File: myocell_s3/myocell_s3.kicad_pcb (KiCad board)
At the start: 4 copper layers, 52 x 71 mm, 100 parts, among them J1 Conn_01x08, J2 IN3P, J3 IN3N, J4 IN4P, J5 Battery Connector JC2, J6 IN4N, J7 USB_C_Receptacle_USB2.0_16P, J8 RLD, Q3 DMG3404L, SW1 SW_Push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

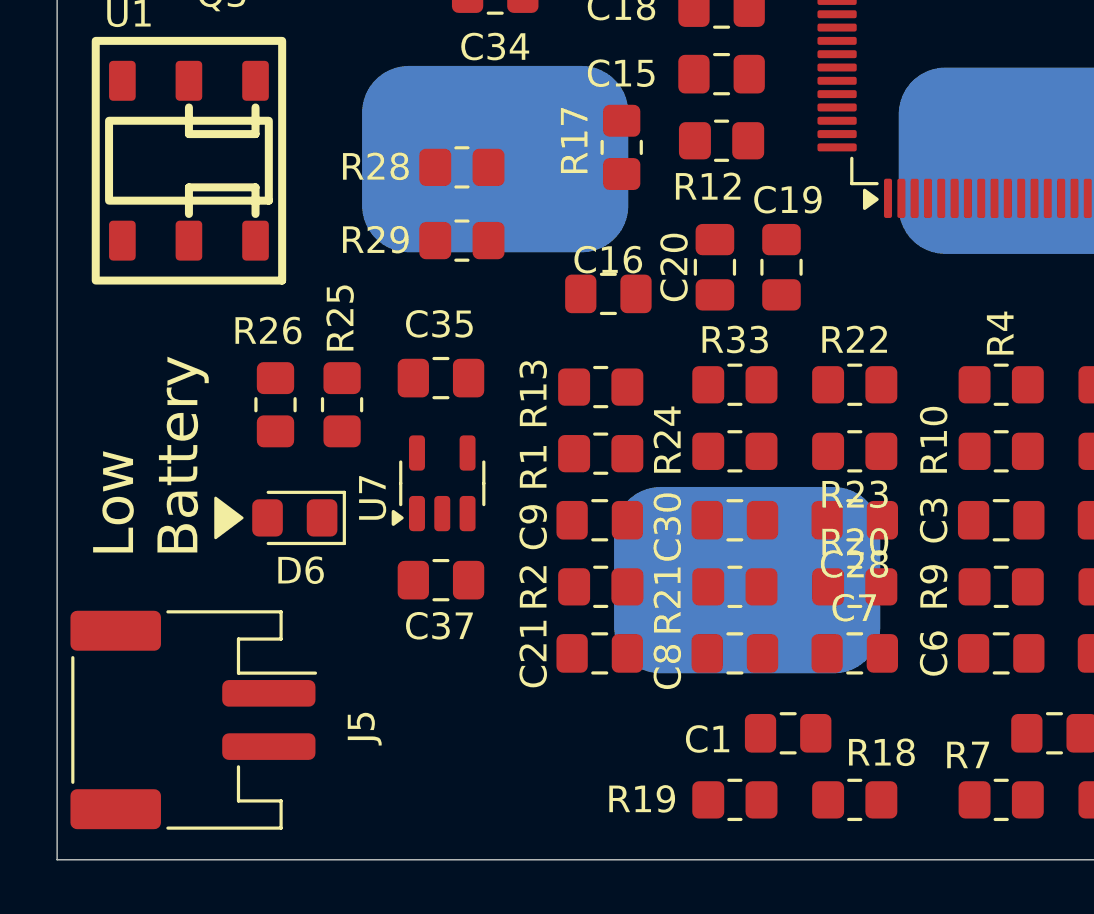
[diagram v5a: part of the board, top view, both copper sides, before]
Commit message: component placement
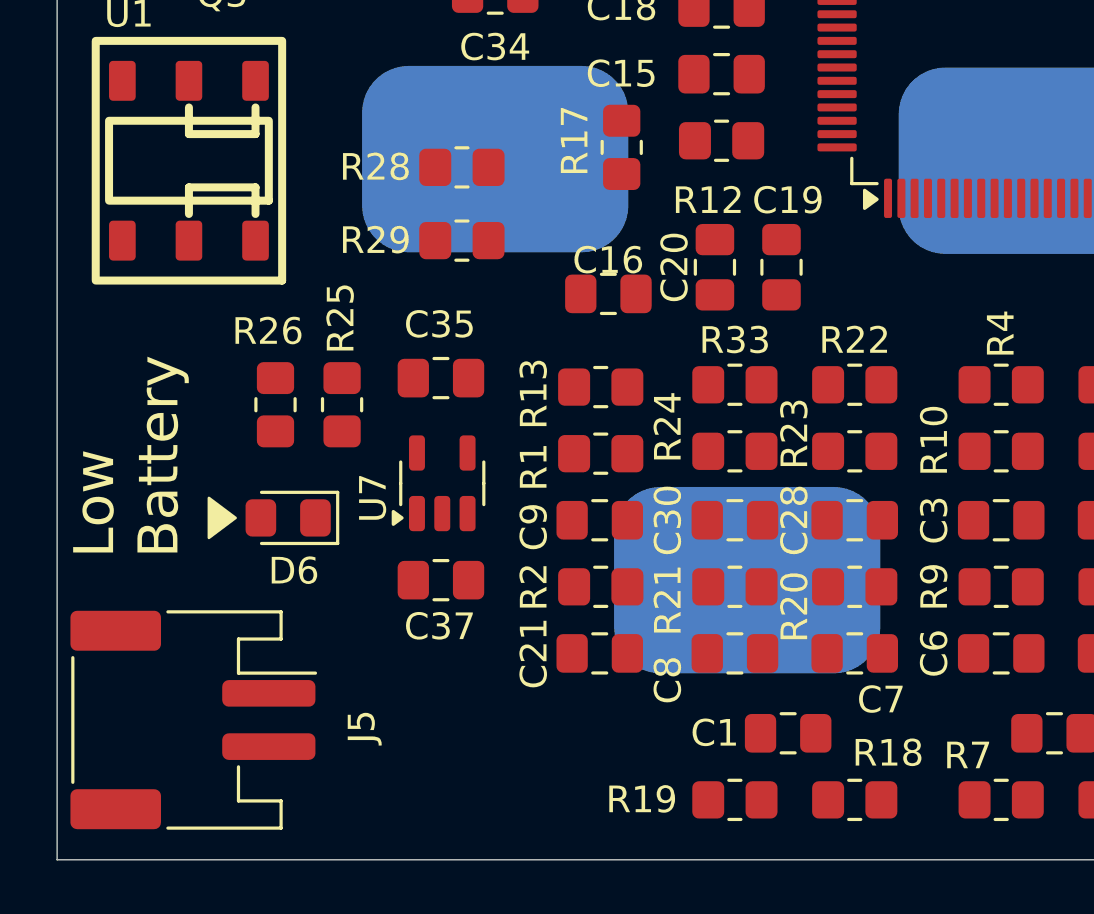
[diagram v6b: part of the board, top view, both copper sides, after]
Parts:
- moved D6 0.25 mm to (162.2, 108.2)
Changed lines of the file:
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@@
 		)
 		(property "Value" "1uF"
-			(at 7.2575 0.5 90)
+			(at -0.261252 -1.5 90)
 			(layer "F.Fab")
 			(effects
@@
 		(tags "resistor handsolder")
 		(property "Reference" "R18"
-			(at -1 1.75 0)
+			(at -1.25 1.75 0)
 			(layer "F.SilkS")
 			(effects
@@
 		(tags "capacitor handsolder")
 		(property "Reference" "C30"
-			(at -2.5 0.25 90)
+			(at -2.5 0 90)
 			(layer "F.SilkS")
 			(effects
@@
 		)
 		(property "Value" "0.1uF"
-			(at 0 1.68 0)
+			(at 2.5 0.25 90)
 			(layer "F.Fab")
 			(effects
@@
 		)
 		(property "Value" "0.01uF"
-			(at -4.25 -2.04 0)
+			(at -5.727064 -1.265 90)
 			(layer "F.Fab")
 			(effects
@@
 		)
 		(property "Value" "4.7uF"
-			(at 0 -5.72 0)
+			(at 0.0375 0.0875 90)
 			(layer "F.Fab")
 			(effects
@@
 		)
 		(fp_text user "${REFERENCE}"
-			(at 0 -3.72 0)
+			(at 0 0.0875 90)
 			(layer "F.Fab")
 			(effects
@@
 		)
 		(property "Value" "0.1uF"
-			(at 2.75 0 90)
+			(at 2.75 0.735 90)
 			(layer "F.Fab")
 			(effects
@@
 		)
 		(fp_text user "${REFERENCE}"
-			(at 0 3.72 0)
+			(at -0.0375 0 90)
 			(layer "F.Fab")
 			(effects
@@
 		)
 		(property "Value" "22k"
-			(at 0 1.65 0)
+			(at -0.227064 0 90)
 			(layer "F.Fab")
 			(effects
@@
 		(tags "resistor handsolder")
 		(property "Reference" "R12"
-			(at -0.5 1.75 0)
+			(at -0.5 2.25 0)
 			(layer "F.SilkS")
 			(effects
@@
 		)
 		(property "Value" "0"
-			(at 0 -2.07 0)
+			(at 0 0 0)
 			(layer "F.Fab")
 			(effects
@@
 		(tags "capacitor handsolder")
 		(property "Reference" "C8"
-			(at -2.5 0.5 90)
+			(at -2.5 1 90)
 			(layer "F.SilkS")
 			(effects
@@
 		)
 		(fp_text user "${REFERENCE}"
-			(at 3.72 0 90)
+			(at 0 0 180)
 			(layer "F.Fab")
 			(effects
@@
 		)
 		(property "Value" "390k"
-			(at 0 5.37 0)
+			(at -0.0375 0 90)
 			(layer "F.Fab")
 			(effects
@@
 		)
 		(property "Value" "1uF"
-			(at 0 5.4 0)
+			(at 0 0 0)
 			(layer "F.Fab")
 			(effects
@@
 		)
 		(fp_text user "${REFERENCE}"
-			(at 0 3.72 0)
+			(at 0 0 90)
 			(layer "F.Fab")
 			(effects
@@
 		)
 		(property "Value" "10k"
-			(at 0 5.37 0)
+			(at 0.227064 0 90)
 			(layer "F.Fab")
 			(effects
@@
 		)
 		(fp_text user "${REFERENCE}"
-			(at 0 3.72 0)
+			(at 0 0 90)
 			(layer "F.Fab")
 			(effects
@@
 		)
 		(property "Value" "2.2uF"
-			(at 3.9625 -0.5 90)
+			(at 2.4625 0.25 180)
 			(layer "F.Fab")
 			(effects
@@
 		)
 		(fp_text user "${REFERENCE}"
-			(at 3.72 0 90)
+			(at -0.0375 0 180)
 			(layer "F.Fab")
 			(effects
@@
 	(footprint "LED_SMD:LED_0805_2012Metric_Pad1.15x1.40mm_HandSolder"
 		(layer "F.Cu")
-		(at 162.475 108.1625 180)
+		(at 162.225 108.1625 180)
 		(descr "LED SMD 0805 (2012 Metric), square (rectangular) end terminal, IPC-7351 nominal, (Body size source: https://docs.google.com/spreadsheets/d/1BsfQQcO9C6DZCsRaXUlFlo91Tg2WpOkGARC1WS5S8t0/edit?usp=sharing), generated with kicad-footprint-generator")
 		(tags "LED handsolder")
@@
 		(tags "resistor handsolder")
 		(property "Reference" "R20"
-			(at 0 -1.65 0)
+			(at -2.25 0.75 90)
 			(layer "F.SilkS")
 			(effects
@@
 		)
 		(property "Value" "0.1uF"
-			(at 6.1825 0 0)
+			(at 0 0.25 0)
 			(layer "F.Fab")
 			(effects
@@
 		)
 		(fp_text user "${REFERENCE}"
-			(at 3.72 0 90)
+			(at 0 0 180)
 			(layer "F.Fab")
 			(effects
@@
 		(tags "resistor handsolder")
 		(property "Reference" "R24"
-			(at 2.5 0.4125 90)
+			(at 2.5 0.9125 90)
 			(layer "F.SilkS")
 			(effects
@@
 		)
 		(fp_text user "${REFERENCE}"
-			(at 3.72 0 90)
+			(at 0 0 180)
 			(layer "F.Fab")
 			(effects
@@
 		(tags "capacitor handsolder")
 		(property "Reference" "C7"
-			(at 0 -1.68 0)
+			(at 1 1.75 180)
 			(layer "F.SilkS")
 			(effects
@@
 		)
 		(property "Value" "4.7uF"
-			(at 0 1.68 0)
+			(at -0.2875 0 90)
 			(layer "F.Fab")
 			(effects
@@
 		(tags "capacitor handsolder")
 		(property "Reference" "C28"
-			(at 0 -1.68 0)
+			(at 2.25 0 90)
 			(layer "F.SilkS")
 			(effects
@@
 		)
 		(fp_text user "${REFERENCE}"
-			(at 3.72 0 90)
+			(at 0 0 180)
 			(layer "F.Fab")
 			(effects
@@
 		(tags "capacitor handsolder")
 		(property "Reference" "C1"
-			(at 3 -0.25 0)
+			(at 2.75 0 0)
 			(layer "F.SilkS")
 			(effects
@@
 		)
 		(property "Value" "20"
-			(at 0 1.65 0)
+			(at 0 -0.735 0)
 			(layer "F.Fab")
 			(effects
@@
 		(tags "resistor handsolder")
 		(property "Reference" "R23"
-			(at 0 -1.65 0)
+			(at 2.25 0.6625 90)
 			(layer "F.SilkS")
 			(effects
@@
 		(at 170 94.69 180)
 		(property "Reference" "J3"
-			(at -7.62 0 0)
+			(at -6.25 0 0)
 			(unlocked yes)
 			(layer "B.SilkS")
@@
 	(gr_poly
 		(pts
-			(xy 159.5 108.9125) (xy 159.5 107.4125) (xy 160.5 108.1625)
+			(xy 159.25 108.9125) (xy 159.25 107.4125) (xy 160.25 108.1625)
 		)
 		(stroke
@@
 	)
 	(gr_text "Low\nBattery"
-		(at 159 109.6625 90)
+		(at 158.25 109.6625 90)
 		(layer "F.SilkS")
 		(effects

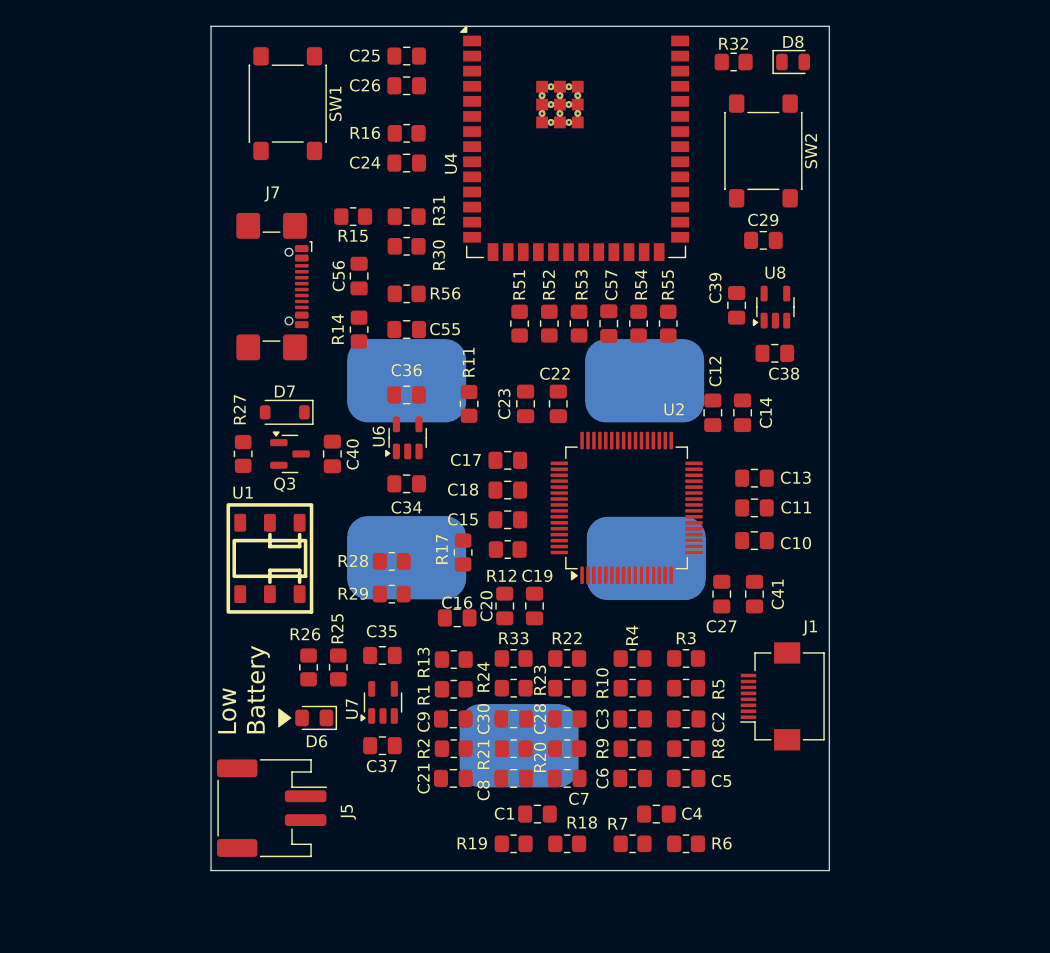
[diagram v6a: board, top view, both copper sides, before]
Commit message: drdy fixed
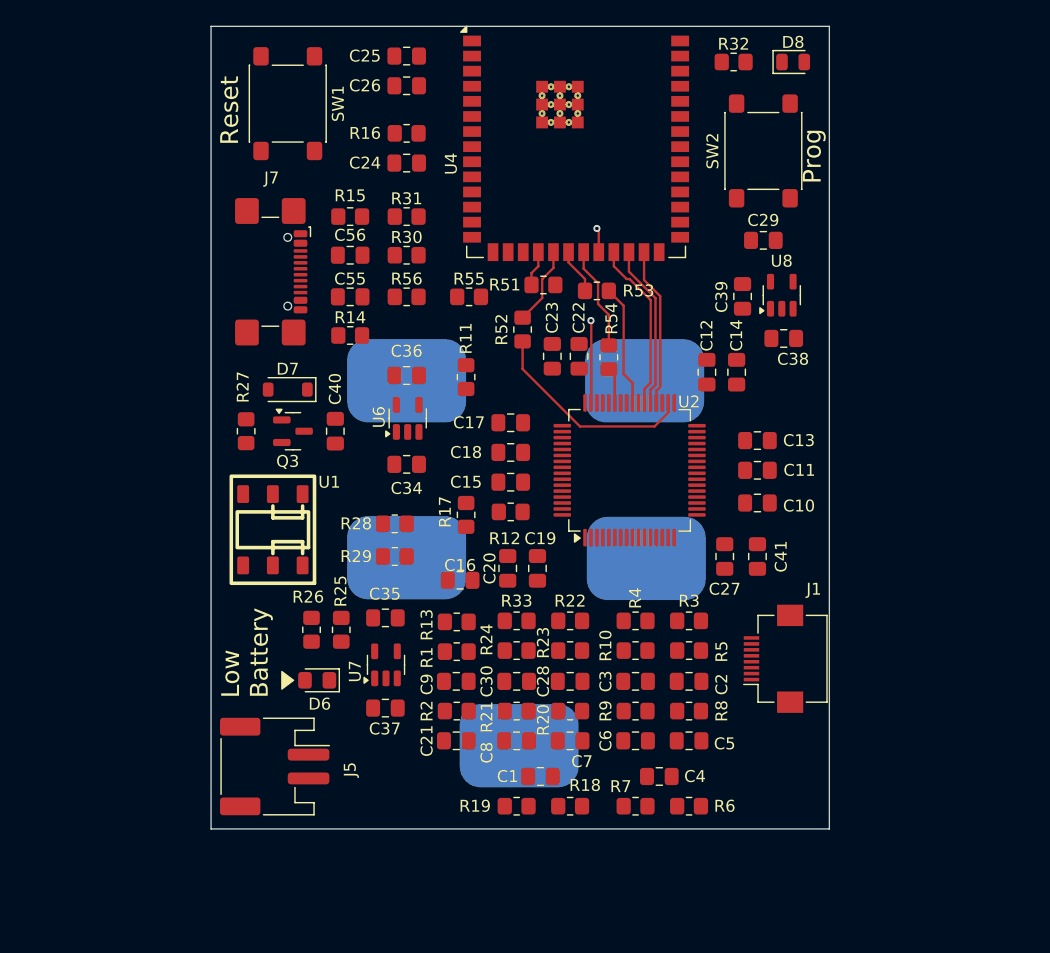
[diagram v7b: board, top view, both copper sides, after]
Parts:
- removed C57: 10pF, Capacitor_SMD:C_0805_2012Metric_Pad1.18x1.45mm_HandSolder
- moved R55 16.9 mm to (175.2, 72.8), turned to 0 degrees
- moved C55 5.49 mm to (165.2, 72.8)
- moved C23 4.59 mm to (182.2, 77.8)
- moved C22 4.37 mm to (184.5, 77.8)
- moved R51 3.82 mm to (181.5, 71.8), turned to 180 degrees
- moved R54 3.78 mm to (187.0, 77.8)
- moved J5 3.51 mm to (158.9, 112.2)
- moved C12 3.45 mm to (195.2, 79.1)
- moved C14 3.45 mm to (197.8, 79.1)
- moved C1 3.17 mm to (181.2, 113.1)
- moved C10 3.17 mm to (199.5, 90.1)
- moved C11 3.17 mm to (199.5, 87.3)
- moved C13 3.17 mm to (199.5, 84.8)
- moved C15 3.17 mm to (178.8, 88.3)
- moved C16 3.17 mm to (174.5, 96.6)
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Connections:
- U4 pad 22: unconnected-(U4-IO14-Pad22) -> /adc_8/drdy
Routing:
- net /adc_8/din: track 0.00 -> 17.9 mm
- net /adc_8/drdy: track 0.00 -> 17.0 mm, vias 0 -> 2
- net /adc_8/start: track 0.00 -> 14.3 mm
- net /adc_8/clk: track 0.00 -> 13.8 mm
- net /adc_8/reset: track 0.00 -> 13.4 mm
- net /adc_8/sclk: track 0.00 -> 10.3 mm
- net Net-(U4-IO13): track 0.00 -> 9.43 mm
- net Net-(U4-IO11): track 0.00 -> 6.93 mm
- net Net-(U4-IO12): track 0.00 -> 3.83 mm
- net /adc_8/dout: track 0.00 -> 3.04 mm
- net Net-(U4-IO10): track 0.00 -> 3.00 mm
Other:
- board size 52 x 71 mm -> 52 x 67.5 mm
- board text added: "Prog"
- board text added: "Reset"

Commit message: spi routed length aligned to 20mm/pm0.5mm
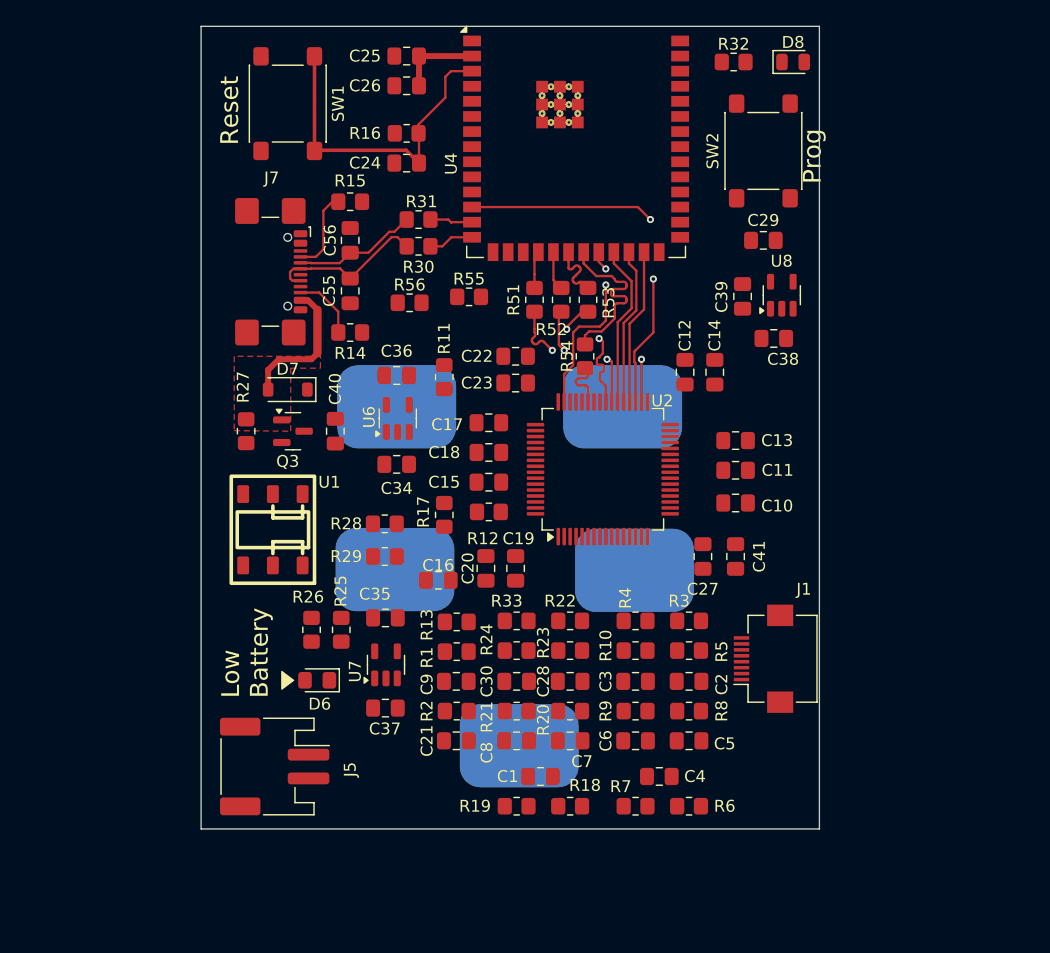
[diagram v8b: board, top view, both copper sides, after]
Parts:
- moved C22 5.34 mm to (179.2, 77.8), turned to 0 degrees
- moved R52 4.10 mm to (183.0, 73.0)
- moved C23 3.82 mm to (179.2, 80.0), turned to 0 degrees
- moved J4 2.87 mm to (188.2, 82.0)
- moved J2 2.34 mm to (169.2, 82.0)
- moved U2 2.25 mm to (186.5, 87.2)
- moved R54 2.00 mm to (185.0, 77.8)
- moved C10 1.84 mm to (197.7, 90.1)
- moved C11 1.84 mm to (197.7, 87.3)
- moved C12 1.84 mm to (193.4, 79.1)
- moved C13 1.84 mm to (197.7, 84.8)
- moved C14 1.84 mm to (195.9, 79.1)
- moved C15 1.84 mm to (176.9, 88.3)
- moved C16 1.84 mm to (172.7, 96.6)
- moved C17 1.84 mm to (176.9, 83.3)
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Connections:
- net Net-(C55-Pad2) renamed /usb_d+
- net Net-(C56-Pad1) renamed /usb_d-
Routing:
- net /adc_8/pwdn: track 0.00 -> 31.6 mm, vias 0 -> 2
- net EN: track 0.00 -> 27.9 mm
- net /adc_8/cs: track 0.00 -> 13.6 mm, vias 0 -> 2
- net /usb_d+: track 0.00 -> 13.5 mm
- net /power_supply/VUSB/2.1A: track 0.00 -> 11.8 mm
- net /usb_d-: track 0.00 -> 10.5 mm
- net Net-(J7-CC1): track 0.00 -> 7.00 mm
- net +3.3V: track 0.00 -> 6.96 mm
- net Net-(U4-IO13): track 9.43 -> 15.1 mm
- net Net-(J7-CC2): track 0.00 -> 5.59 mm
- net /cpu_wroom_esp32/D+: track 0.00 -> 3.81 mm
- net /adc_8/din: track 17.9 -> 14.1 mm, vias 0 -> 2
- net Net-(U4-IO11): track 6.93 -> 3.28 mm
- net /cpu_wroom_esp32/D-: track 0.00 -> 3.62 mm
- net /adc_8/sclk: track 10.3 -> 12.5 mm, vias 0 -> 2
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- added copper zone on F.Cu, net /power_supply/VUSB/2.1A
